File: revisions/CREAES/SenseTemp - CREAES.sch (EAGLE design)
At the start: 46 parts, among them Q1 mmbt2222, U1 MIC5225-3.3, U2 AT21CS01, U3 MAX31865, U4 MAX31865, U5 MAX31865, U6 MAX31865

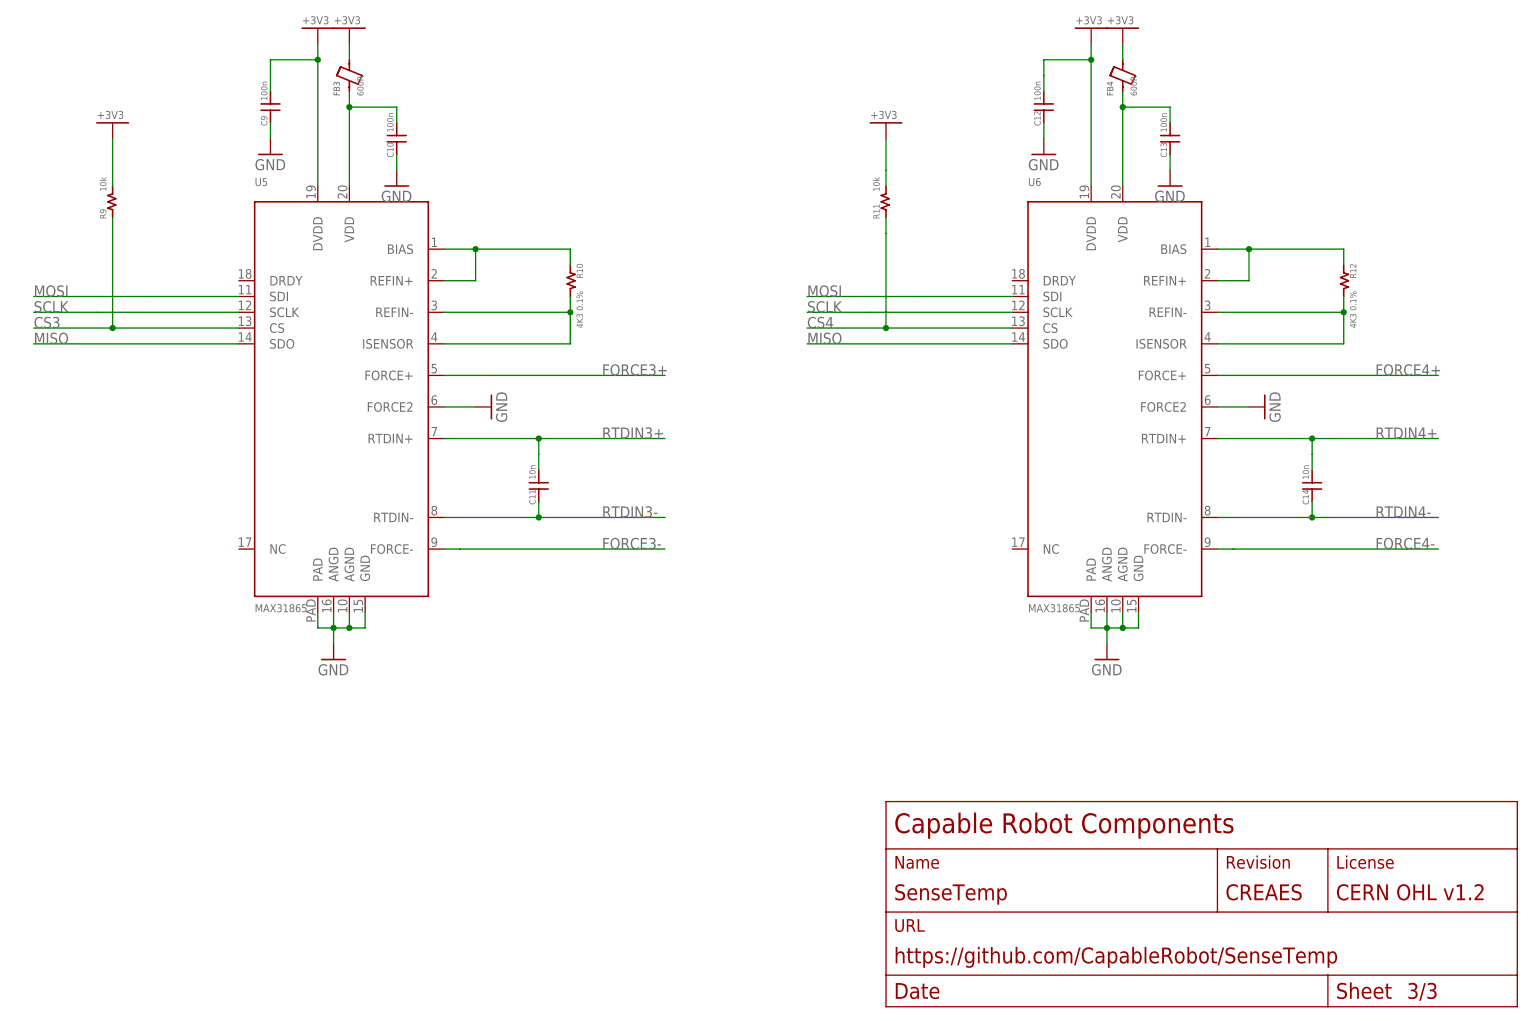
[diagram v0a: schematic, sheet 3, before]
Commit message: Change silk screen around RTD connector
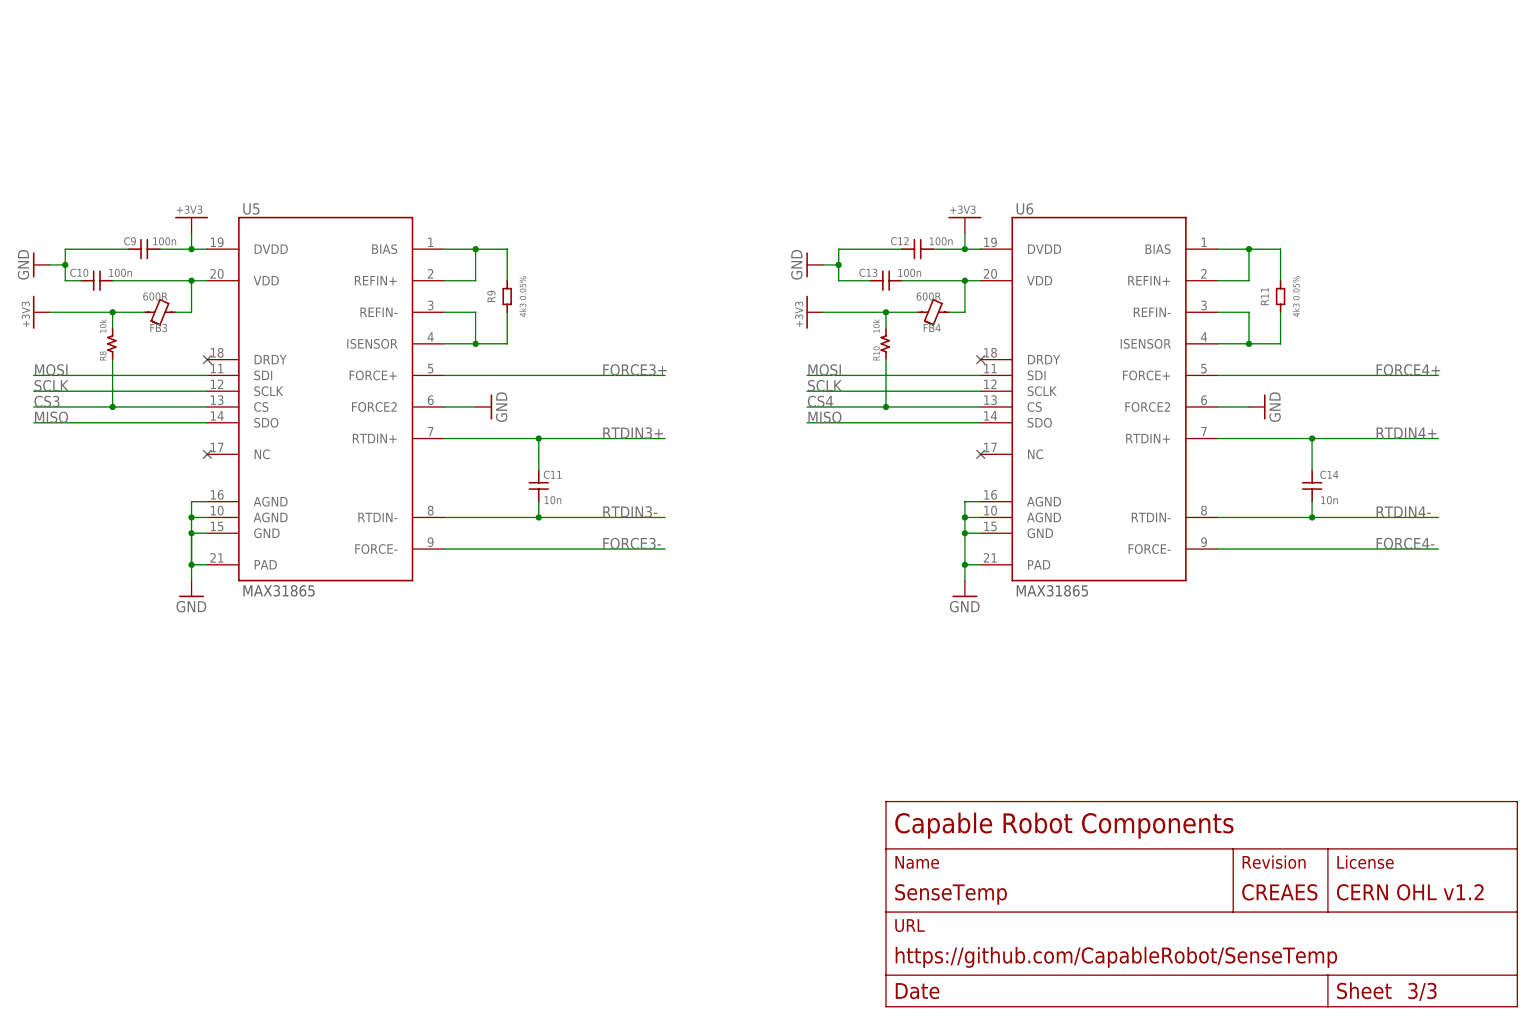
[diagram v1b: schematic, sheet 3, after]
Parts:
- removed ACT: (no value), SparkFun-LED:LED0603
- removed C1, C2: 10u, CapableRobot:CAP1206
- removed FID1, FID2: FIDUCIAL"", microbuilder:FIDUCIAL""
- removed J1: (no value), SparkFun-Connectors:CONN_12NO_SILK
- removed J2: (no value), SparkFun-Connectors:CONN_161X16_NO_SILK
- removed R13: 1k, CapableRobot:RES0603
- removed U1: MIC5225-3.3, microbuilder:VREG_SOT23-5
- added C15, C16: 10u, CapableRobot:CAP0805
- added D1: MBR120, Adafruit Feather M0 Express:DIODE-SCHOTTKYSOD-123
- added J3: FEATHERPTH, CapableRobot:FEATHERPTH
- added Q2: DMP2045, Adafruit Feather M4 Express:MOSFET-P
- added R16: 10k, CapableRobot:RES0603
- added U7: 3v3, CapableRobot:MIC5225
- LOGO1: value CRC-LOGO10 -> CRC-LOGO7SILK; device CapableRobot:CRC-LOGO10 -> CapableRobot:CRC-LOGO7SILK
- Q1: value mmbt2222 -> MMBT2222; device SparkFun-DiscreteSemi:TRANS_NPN-MMBT2222AL -> Adafruit HUZZAH32 ESP32 Feather:TRANSISTOR_NPNSOT23-3; MPN (none) -> MMBT2222LT1G
- R10, R6, R8: value 4K3 0.1% -> 10k
- R11, R5, R7, R9: value 10k -> 4k3 0.05%
- R12: value 4K3 0.1% -> 100k
- R2: value 10k -> 1k
- R4: value 1k -> 10k
- RTD1: MPN (none) -> 3221-16-0300-00
- U3, U4, U5, U6: device microbuilder:TEMP_MAX31865 -> CapableRobot:MAX31865
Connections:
- removed net +5V: C1.P$2, J1.3, R2.2, U1.IN
- removed net LED: J2.1, R13.1
- removed net N$17 (its old number): R3.1, R4.2
- removed net N$18: ACT.A, R13.2
- removed net N$3: Q1.C, R2.1, U1.EN
- new net EN: Q1.C, R16.2, U7.EN
- new net N$4: R2.1, R3.2
- new net VBAT: J3.BAT, Q2.D
- new net VBUS: D1.A, J3.USB, Q2.G, R12.2
- new net VIN: C15.P$2, D1.C, Q2.S, R16.1, U7.IN
- net !EN: now also J3.5; no longer J1.4
- net +3V3: now also C12.P$1, C16.P$2, C3.P$1, C6.P$1, C9.P$1, R10.2, R2.2, R4.2, R6.2, R8.2, U7.OUT; no longer C12.P$2, C2.P$2, C3.P$2, C6.P$2, C9.P$2, R11.2, R3.2, R5.2, R7.2, R9.2, U1.OUT
- net CS1: now also J3.4, R4.1; no longer J1.7, R5.1
- net CS2: now also J3.3, R6.1; no longer J1.8, R7.1
- net CS3: now also J3.2, R8.1; no longer J1.9, R9.1
- net CS4: now also J3.1, R10.1; no longer J1.10, R11.1
- net GND: now also C10.P$2, C12.P$2, C13.P$2, C15.P$1, C16.P$1, C3.P$2, C4.P$2, C6.P$2, C7.P$2, C9.P$2, J3.GND, R12.1, U3.AGND@1, U4.AGND@1, U5.AGND@1, U6.AGND@1, U7.GND; no longer ACT.C, C1.P$1, C10.P$1, C12.P$1, C13.P$1, C2.P$1, C3.P$1, C4.P$1, C6.P$1, C7.P$1, C9.P$1, J2.13, U1.GND, U3.ANGD@1, U4.ANGD@1, U5.ANGD@1, U6.ANGD@1
- net MISO: now also J3.MISO; no longer J2.4
- net MOSI: now also J3.MOSI; no longer J2.5
- net N$10: now also C7.P$1; no longer C7.P$2
- net N$11: now also R9.2; no longer R10.1
- net N$12: now also R9.1; no longer R10.2
- net N$13: now also C10.P$1; no longer C10.P$2
- net N$14: now also R11.2; no longer R12.1
- net N$15: now also R11.1; no longer R12.2
- net N$16: now also C13.P$1; no longer C13.P$2
- net N$5: now also R5.2; no longer R6.1
- net N$6: now also R5.1; no longer R6.2
- net N$7: now also C4.P$1; no longer C4.P$2
- net N$8: now also R7.2; no longer R8.2
- net N$9: now also R7.1; no longer R8.1
- net RTDIN1+: now also C5.P$1; no longer C5.P$2
- net RTDIN1-: now also C5.P$2; no longer C5.P$1
- net RTDIN2+: now also C8.P$1; no longer C8.P$2
- net RTDIN2-: now also C8.P$2; no longer C8.P$1
- net RTDIN3+: now also C11.P$1; no longer C11.P$2
- net RTDIN3-: now also C11.P$2; no longer C11.P$1
- net RTDIN4+: now also C14.P$1; no longer C14.P$2
- net RTDIN4-: now also C14.P$2; no longer C14.P$1
- net SCLK: now also J3.SCK; no longer J2.6
- net SIO: now also J3.6, R3.1; no longer J1.5, R4.1
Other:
- moved on the sheet: C10, C11, C12, C13, C14, C3, C4, C5, C6, C7, C8, C9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
